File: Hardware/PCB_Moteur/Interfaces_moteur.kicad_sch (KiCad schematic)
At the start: 50 parts, among them J10 Conn_01x02, J11 Conn_01x02, J12 Conn_01x02, J13 Conn_01x02, J14 Conn_01x02, J15 Conn_01x02, J16 Conn_01x06_Pin, J3 Conn_01x03_Socket, J4 Conn_01x03_Socket, J5 Conn_01x03_Socket, J6 Conn_01x03_Socket, J7 Conn_01x02, J8 Conn_01x02, J9 Conn_01x02, U3 MCP1802T-5002I/OT, U4 LSF0204PWR, U5 ISOW1044

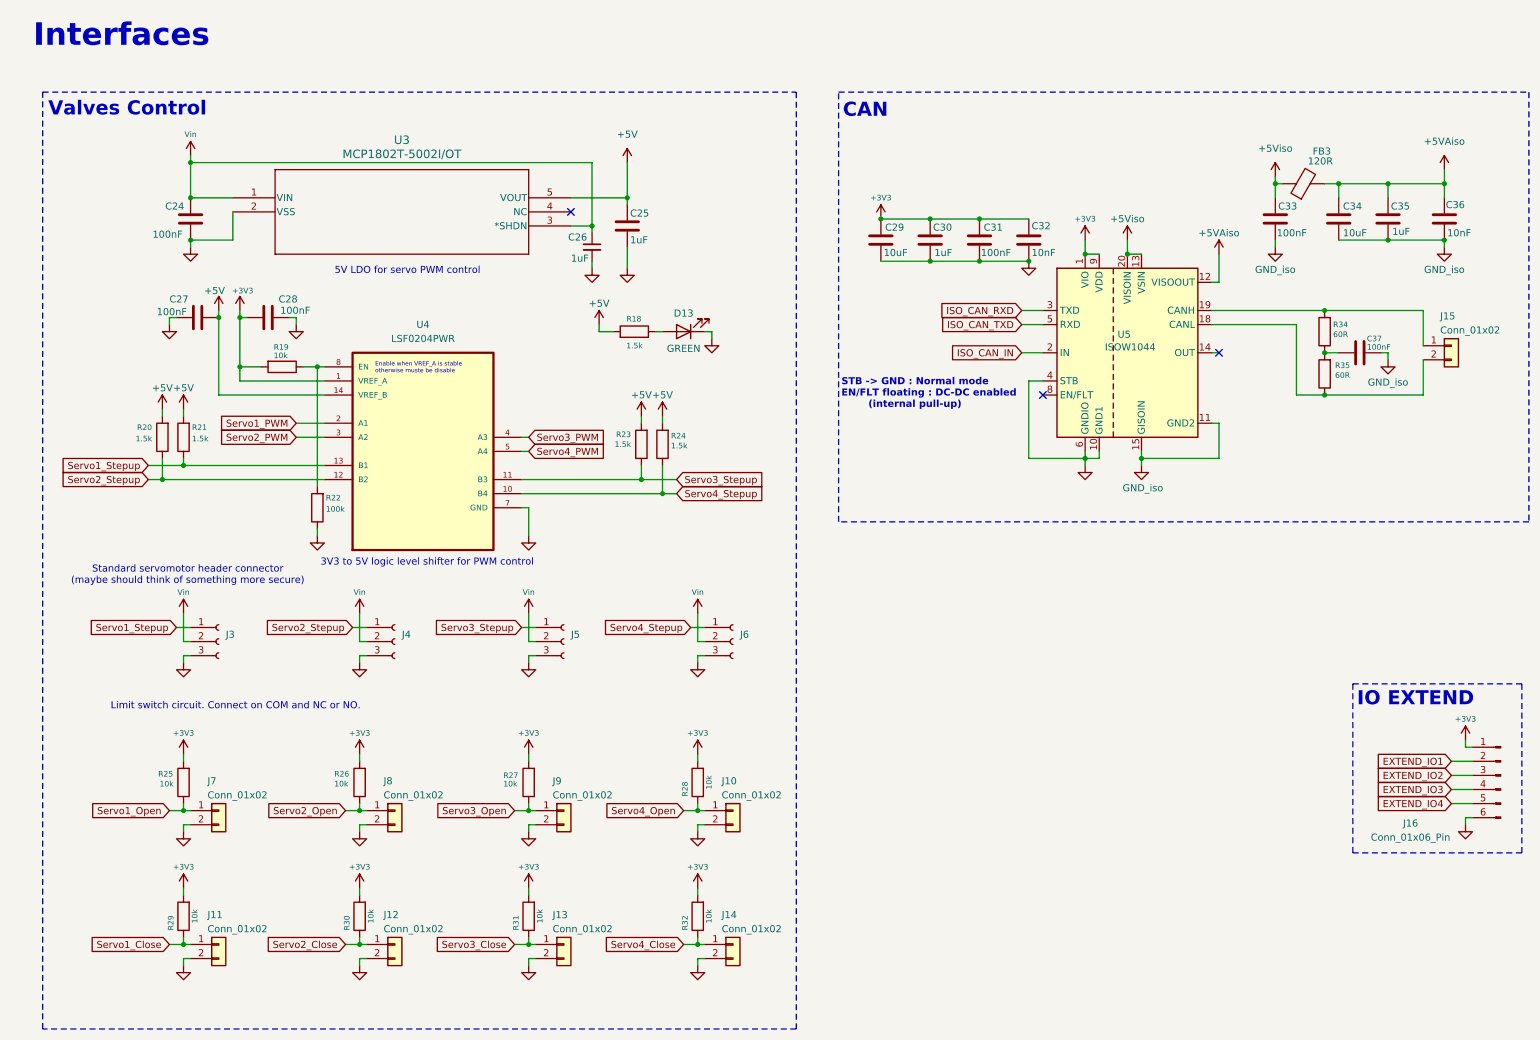
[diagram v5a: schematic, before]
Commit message: fix: symbols refactorisation (footprint missing)
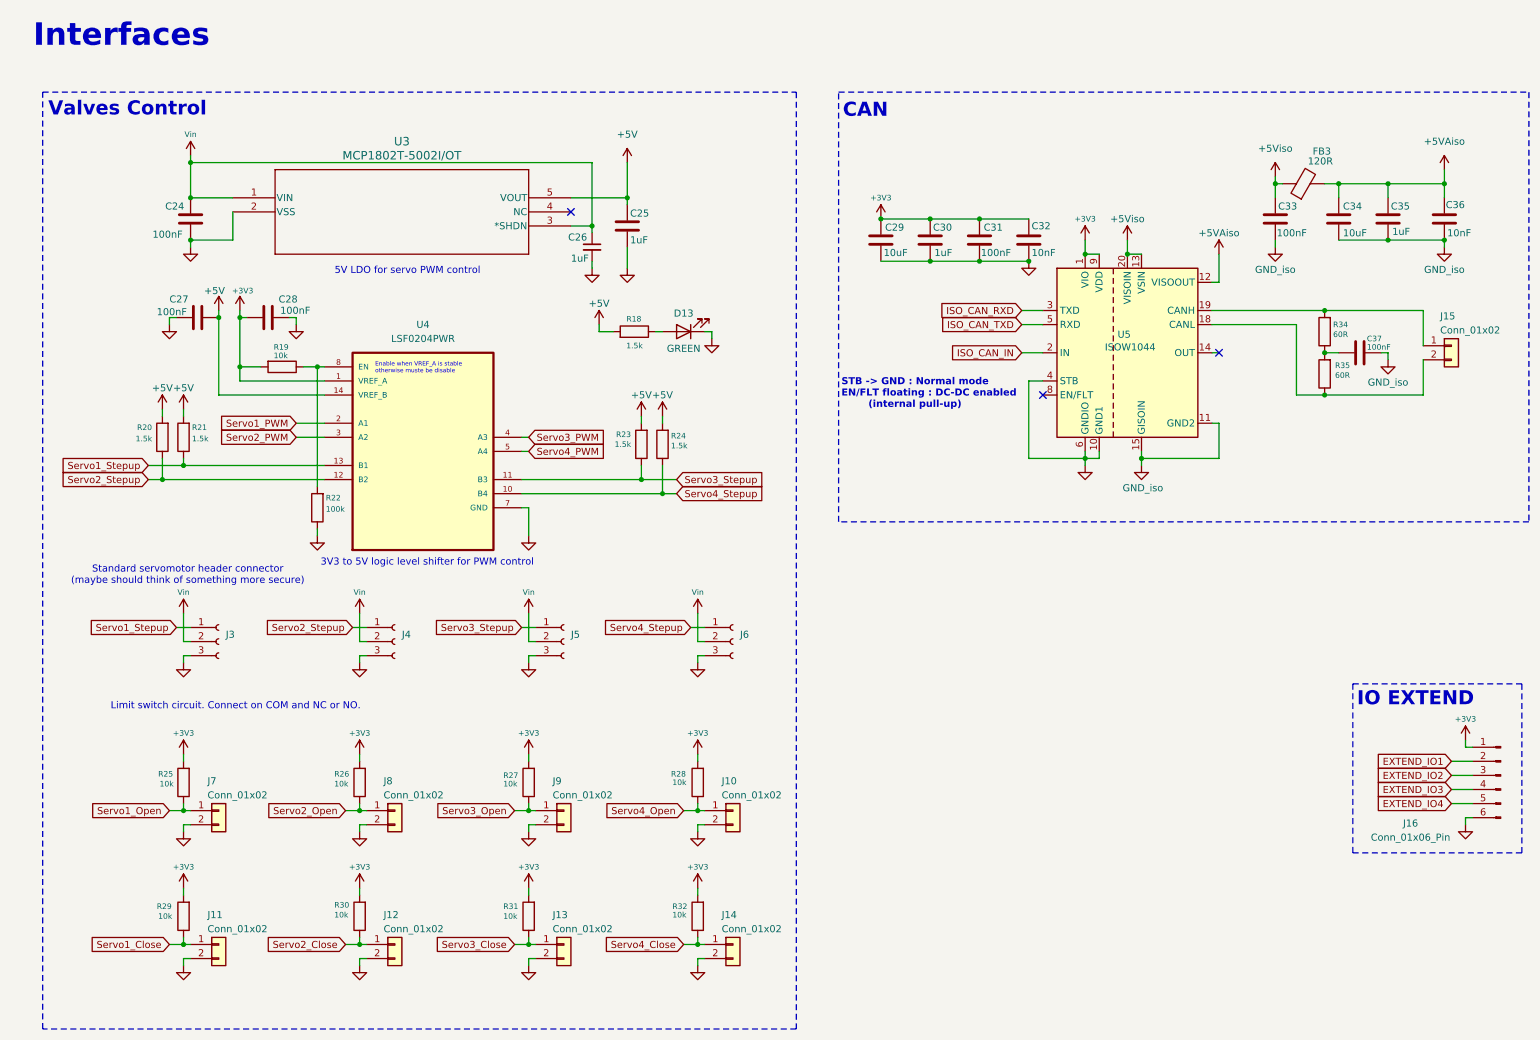
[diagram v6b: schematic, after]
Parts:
- removed U3: MCP1802T-5002I/OT, Package_TO_SOT_SMD:SOT-23-5, symbol 2026-01-14_15-06-07:MCP1802T-5002I_OT
- added U3: MCP1802T-5002I/OT, SOT-23-5_MC_MCH, symbol pcb_moteur:MCP1802T-5002I_OT
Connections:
- net +5V: now also U3.5 (VOUT)
- net GND: now also U3.2 (VSS)
- net Vin: now also U3.1 (VIN), U3.3 (*SHDN)
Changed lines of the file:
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@@
 		(dnp no)
 		(property "Reference" "R30"
-			(at 70.104 177.8 90)
+			(at 67.818 173.228 0)
 			(effects
 				(font
@@
 		)
 		(property "Value" "10k"
-			(at 74.422 176.53 90)
+			(at 67.818 175.006 0)
 			(effects
 				(font
@@
 		(dnp no)
 		(property "Reference" "R31"
-			(at 100.584 177.8 90)
+			(at 98.298 173.482 0)
 			(effects
 				(font
@@
 		)
 		(property "Value" "10k"
-			(at 104.902 176.53 90)
+			(at 98.298 175.26 0)
 			(effects
 				(font
@@
 	)
 	(symbol
+		(lib_id "pcb_moteur:MCP1802T-5002I_OT")
+		(at 49.53 45.72 0)
+		(unit 1)
+		(exclude_from_sim no)
+		(in_bom yes)
+		(on_board yes)
+		(dnp no)
+		(fields_autoplaced yes)
+		(property "Reference" "U3"
+			(at 80.01 35.56 0)
+			(effects
+				(font
+					(size 1.524 1.524)
+				)
+			)
+		)
+		(property "Value" "MCP1802T-5002I/OT"
+			(at 80.01 38.1 0)
+			(effects
+				(font
+					(size 1.524 1.524)
+				)
+			)
+		)
+		(property "Footprint" "SOT-23-5_MC_MCH"
+			(at 49.53 45.72 0)
+			(effects
+				(font
+					(size 1.27 1.27)
+					(italic yes)
+				)
+				(hide yes)
+			)
+		)
+		(property "Datasheet" "MCP1802T-5002I/OT"
+			(at 49.53 45.72 0)
+			(effects
+				(font
+					(size 1.27 1.27)
+					(italic yes)
+				)
+				(hide yes)
+			)
+		)
+		(property "Description" ""
+			(at 49.53 45.72 0)
+			(effects
+				(font
+					(size 1.27 1.27)
+				)
+				(hide yes)
+			)
+		)
+		(pin "3"
+		)
+		(pin "2"
+		)
+		(pin "5"
+		)
+		(pin "1"
+		)
+		(pin "4"
+		)
+		(instances
+			(project ""
+				(path "/b0d87684-7b1c-41d8-8358-755aa327573e/a8ed0c04-b51e-4eec-84d1-0b2303d57d27"
+					(reference "U3")
+					(unit 1)
+				)
+			)
+		)
+	)
+	(symbol
 		(lib_id "Connector:Conn_01x03_Socket")
 		(at 78.74 125.73 0)
@@
 		(dnp no)
 		(property "Reference" "R29"
-			(at 38.354 177.8 90)
+			(at 35.814 173.482 0)
 			(effects
 				(font
@@
 		)
 		(property "Value" "10k"
-			(at 42.672 176.53 90)
+			(at 36.068 175.26 0)
 			(effects
 				(font
@@
 		(dnp no)
 		(property "Reference" "R28"
-			(at 131.064 153.67 90)
+			(at 128.524 149.606 0)
 			(effects
 				(font
@@
 		)
 		(property "Value" "10k"
-			(at 135.382 152.4 90)
+			(at 128.778 151.13 0)
 			(effects
 				(font
@@
 	)
 	(symbol
-		(lib_id "2026-01-14_15-06-07:MCP1802T-5002I_OT")
-		(at 49.53 45.72 0)
-		(unit 1)
-		(exclude_from_sim no)
-		(in_bom yes)
-		(on_board yes)
-		(dnp no)
-		(property "Reference" "U3"
-			(at 80.01 35.306 0)
-			(effects
-				(font
-					(size 1.524 1.524)
-				)
-			)
-		)
-		(property "Value" "MCP1802T-5002I/OT"
-			(at 80.01 37.846 0)
-			(effects
-				(font
-					(size 1.524 1.524)
-				)
-			)
-		)
-		(property "Footprint" "Package_TO_SOT_SMD:SOT-23-5"
-			(at 49.53 45.72 0)
-			(effects
-				(font
-					(size 1.27 1.27)
-					(italic yes)
-				)
-				(hide yes)
-			)
-		)
-		(property "Datasheet" "MCP1802T-5002I/OT"
-			(at 49.53 45.72 0)
-			(effects
-				(font
-					(size 1.27 1.27)
-					(italic yes)
-				)
-				(hide yes)
-			)
-		)
-		(property "Description" "https://www.digikey.ca/en/products/detail/microchip-technology/MCP1802T-5002I-OT/1679145"
-			(at 49.53 45.72 0)
-			(effects
-				(font
-					(size 1.27 1.27)
-				)
-				(hide yes)
-			)
-		)
-		(property "DigiKey_Part_Number" "MCP1802T-5002I/OTCT-ND"
-			(at 49.53 45.72 0)
-			(effects
-				(font
-					(size 1.27 1.27)
-				)
-				(hide yes)
-			)
-		)
-		(property "Manufacturer_Part_Number" "MCP1802T-5002I/OT"
-			(at 49.53 45.72 0)
-			(effects
-				(font
-					(size 1.27 1.27)
-				)
-				(hide yes)
-			)
-		)
-		(pin "5"
-		)
-		(pin "4"
-		)
-		(pin "2"
-		)
-		(pin "3"
-		)
-		(pin "1"
-		)
-		(instances
-			(project "PCB_moteur"
-				(path "/b0d87684-7b1c-41d8-8358-755aa327573e/a8ed0c04-b51e-4eec-84d1-0b2303d57d27"
-					(reference "U3")
-					(unit 1)
-				)
-			)
-		)
-	)
-	(symbol
 		(lib_id "Device:R")
 		(at 133.35 175.26 180)
@@
 		(dnp no)
 		(property "Reference" "R32"
-			(at 131.064 177.8 90)
+			(at 128.778 173.482 0)
 			(effects
 				(font
@@
 		)
 		(property "Value" "10k"
-			(at 135.382 176.53 90)
+			(at 128.778 175.006 0)
 			(effects
 				(font

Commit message: wip : done all footprints
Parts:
- added C? (x4): 10uF, Capacitor_SMD:C_0805_2012Metric, symbol Device:C
- D13: footprint ODB:LED_QBLP601-AG15 -> pcb_moteur:LED_QBLP601-AG15
- J10, J11, J12, J13, J14, J7, J8, J9: footprint (none) -> pcb_moteur:TE_640454-2
- J15: footprint (none) -> pcb_moteur:CONN_2189890010-SD_02_MOL
- J16: footprint (none) -> Connector_PinSocket_2.54mm:PinSocket_2x03_P2.54mm_Vertical
- U3: footprint SOT-23-5_MC_MCH -> pcb_moteur:MCP1802T-5002IOT
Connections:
- net GND: now also C?.2, C?.2, C?.2, C?.2
- net Vin: now also C?.1, C?.1, C?.1, C?.1

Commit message: wip : add final footprint to lib and start pcb
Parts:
- gave numbers to parts that had none: 4
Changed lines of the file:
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@@
 		(on_board yes)
 		(dnp no)
-		(property "Reference" "C?"
+		(property "Reference" "C50"
 			(at 32.512 127.254 0)
 			(effects
@@
 			(project "PCB_moteur"
 				(path "/b0d87684-7b1c-41d8-8358-755aa327573e/a8ed0c04-b51e-4eec-84d1-0b2303d57d27"
-					(reference "C?")
+					(reference "C50")
 					(unit 1)
 				)
@@
 		(on_board yes)
 		(dnp no)
-		(property "Reference" "C?"
+		(property "Reference" "C51"
 			(at 64.262 127.254 0)
 			(effects
@@
 			(project "PCB_moteur"
 				(path "/b0d87684-7b1c-41d8-8358-755aa327573e/a8ed0c04-b51e-4eec-84d1-0b2303d57d27"
-					(reference "C?")
+					(reference "C51")
 					(unit 1)
 				)
@@
 		(on_board yes)
 		(dnp no)
-		(property "Reference" "C?"
+		(property "Reference" "C53"
 			(at 125.222 127.254 0)
 			(effects
@@
 			(project "PCB_moteur"
 				(path "/b0d87684-7b1c-41d8-8358-755aa327573e/a8ed0c04-b51e-4eec-84d1-0b2303d57d27"
-					(reference "C?")
+					(reference "C53")
 					(unit 1)
 				)
@@
 		(on_board yes)
 		(dnp no)
-		(property "Reference" "C?"
+		(property "Reference" "C52"
 			(at 94.742 127.254 0)
 			(effects
@@
 			(project "PCB_moteur"
 				(path "/b0d87684-7b1c-41d8-8358-755aa327573e/a8ed0c04-b51e-4eec-84d1-0b2303d57d27"
-					(reference "C?")
+					(reference "C52")
 					(unit 1)
 				)
